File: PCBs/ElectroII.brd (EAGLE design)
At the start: 114.3 x 76.2 mm, 35 parts, among them J1 U.FL-R-SMT(01), T1 VIN, T2 VBAT, T3 GND, T4 5V, T5 VCC, U1 RFM95W-868S2, U2 TPS61090RSAR

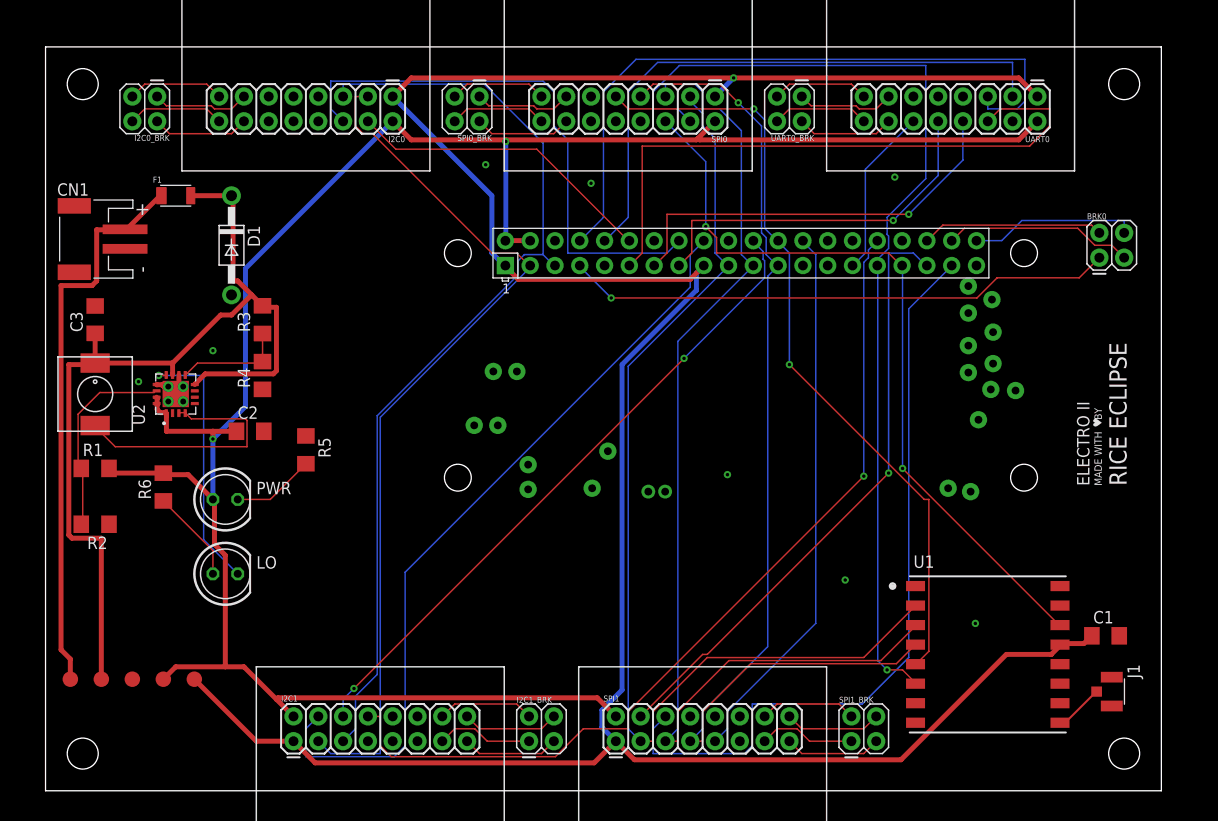
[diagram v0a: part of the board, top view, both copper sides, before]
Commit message: Fixed MOSI/MISO mistake
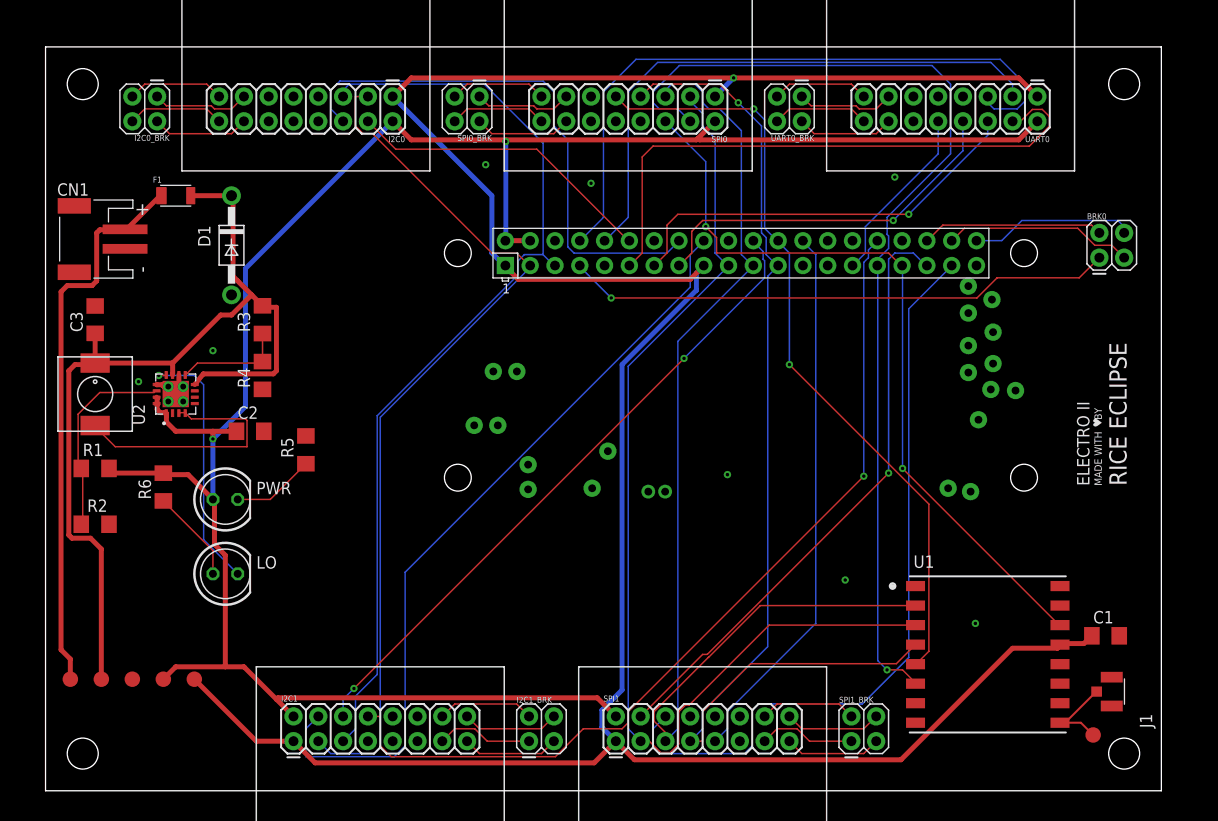
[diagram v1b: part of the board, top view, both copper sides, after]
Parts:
- added T6: ANT, RTR Main Library:TEST_PAD
- C2: value 100u -> 47u
- R1: value 1.85M -> 1.8M
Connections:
- net ANT: now also T6.P$1
- net MISO: now also U1.2; no longer U1.3
- net MOSI: now also U1.3; no longer U1.2
- net UART0_GPIO0: now also UART0.4; no longer UART0.6
- net UART0_GPIO1: now also UART0.6; no longer UART0.8
- net UART0_GPIO2: now also UART0.8; no longer UART0.10
- net UART0_GPIO3: now also UART0.10; no longer UART0.12
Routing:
- net ANT: track 5.07 -> 8.98 mm
- net UART0_GPIO0: track 64.0 -> 60.3 mm
- net SPI0_GPIO0: track 103.2 -> 105.3 mm
- net TX: track 70.5 -> 68.7 mm
- net MISO: track 111.2 -> 112.9 mm
- net RX: track 60.4 -> 59.1 mm
- net VBAT: track 95.4 -> 94.2 mm
- net UART0_GPIO3: track 17.4 -> 18.4 mm
- net I2C0_GPIO1: track 57.0 -> 56.1 mm
- net SPI1_GPIO1: track 79.1 -> 78.3 mm
- net 5V: track 222.9 -> 222.4 mm
- net VIN: track 57.9 -> 57.3 mm
- net N$2: track 27.2 -> 26.6 mm

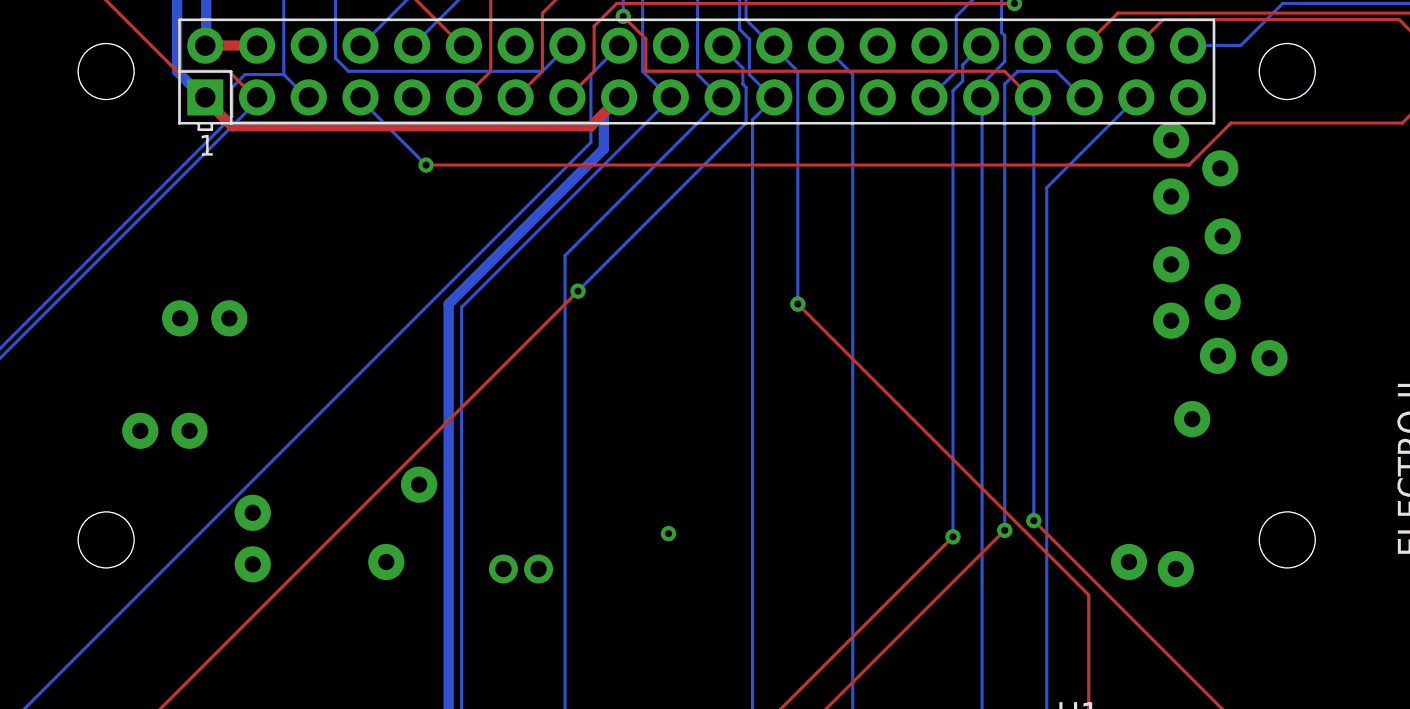
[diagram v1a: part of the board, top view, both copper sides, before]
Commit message: Updated RPi library
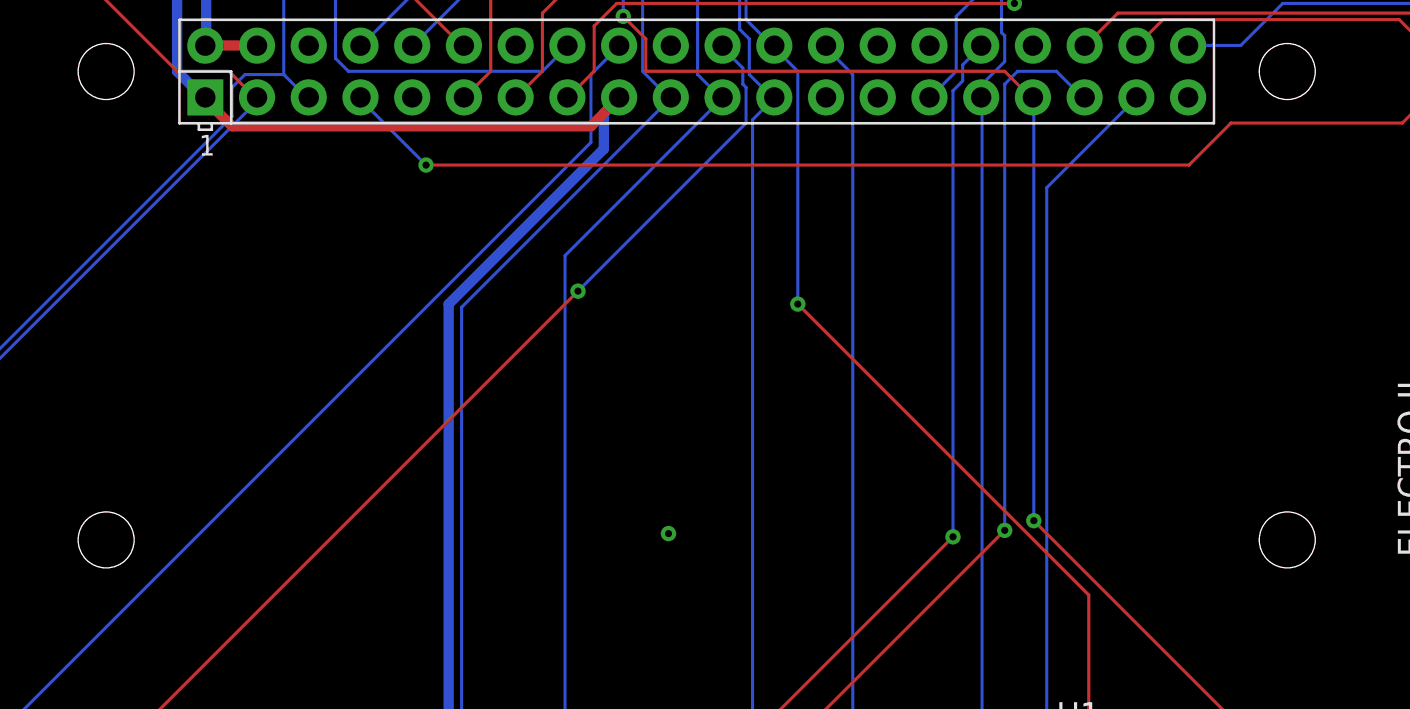
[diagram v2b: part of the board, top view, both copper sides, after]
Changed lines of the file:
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@@
 <wire x1="11.94450625" y1="41.5922" x2="12.13470625" y2="41.402" width="0.508" layer="1"/>
 <wire x1="12.13470625" y1="41.402" x2="12.573" y2="41.402" width="0.508" layer="1"/>
+<wire x1="86.995" y1="62.865" x2="88.9" y2="71.12" width="0" layer="19" extent="1-1"/>
+<wire x1="87.745" y1="56.345" x2="86.995" y2="62.865" width="0" layer="19" extent="1-1"/>
+<wire x1="82.665" y1="56.345" x2="87.745" y2="56.345" width="0" layer="19" extent="1-1"/>
+<wire x1="77.585" y1="53.805" x2="82.665" y2="56.345" width="0" layer="19" extent="1-1"/>
+<wire x1="95.365" y1="53.805" x2="87.745" y2="56.345" width="0" layer="19" extent="1-1"/>
+<wire x1="69.965" y1="56.345" x2="77.585" y2="53.805" width="0" layer="19" extent="1-1"/>
+<wire x1="62.345" y1="56.345" x2="69.965" y2="56.345" width="0" layer="19" extent="1-1"/>
+<wire x1="57.265" y1="53.805" x2="62.345" y2="56.345" width="0" layer="19" extent="1-1"/>
+<wire x1="52.185" y1="56.345" x2="57.265" y2="53.805" width="0" layer="19" extent="1-1"/>
+<wire x1="55.88" y1="62.23" x2="52.185" y2="56.345" width="0" layer="19" extent="1-1"/>
+<wire x1="55.88" y1="71.12" x2="55.88" y2="62.23" width="0" layer="19" extent="1-1"/>
+<wire x1="45.085" y1="64.135" x2="52.185" y2="56.345" width="0" layer="19" extent="1-1"/>
+<wire x1="69.85" y1="32.385" x2="77.585" y2="53.805" width="0" layer="19" extent="1-1"/>
+<wire x1="81.915" y1="21.59" x2="69.85" y2="32.385" width="0" layer="19" extent="1-1"/>
+<wire x1="89.12" y1="20.97" x2="81.915" y2="21.59" width="0" layer="19" extent="1-1"/>
+<wire x1="95.25" y1="17.145" x2="89.12" y2="20.97" width="0" layer="19" extent="1-1"/>
+<wire x1="89.12" y1="6.97" x2="95.25" y2="17.145" width="0" layer="19" extent="1-1"/>
+<wire x1="103.92" y1="8.97" x2="95.25" y2="17.145" width="0" layer="19" extent="1-1"/>
+<wire x1="109.22" y1="8.685" x2="103.92" y2="8.97" width="0" layer="19" extent="1-1"/>
+<wire x1="109.22" y1="11.635" x2="109.22" y2="8.685" width="0" layer="19" extent="1-1"/>
+<wire x1="109.985" y1="15.875" x2="109.22" y2="11.635" width="0" layer="19" extent="1-1"/>
+<wire x1="71.12" y1="5.08" x2="89.12" y2="6.97" width="0" layer="19" extent="1-1"/>
+<wire x1="22.86" y1="71.12" x2="45.085" y2="64.135" width="0" layer="19" extent="1-1"/>
+<wire x1="19.05" y1="50.8" x2="22.86" y2="71.12" width="0" layer="19" extent="1-1"/>
+<wire x1="17.145" y1="45.085" x2="19.05" y2="50.8" width="0" layer="19" extent="1-1"/>
+<wire x1="13.66" y1="42.595" x2="17.145" y2="45.085" width="0" layer="19" extent="1-1"/>
+<wire x1="13.335" y1="40.64" x2="14.097" y2="41.402" width="0" layer="19" extent="1-1"/>
+<wire x1="14.097" y1="39.878" x2="13.335" y2="40.64" width="0" layer="19" extent="1-1"/>
+<wire x1="12.573" y1="39.878" x2="13.335" y2="40.64" width="0" layer="19" extent="1-1"/>
+<wire x1="15.29" y1="39.665" x2="14.097" y2="39.878" width="0" layer="19" extent="1-1"/>
+<wire x1="15.29" y1="40.315" x2="15.29" y2="39.665" width="0" layer="19" extent="1-1"/>
+<wire x1="15.29" y1="40.965" x2="15.29" y2="40.315" width="0" layer="19" extent="1-1"/>
+<wire x1="9.525" y1="41.91" x2="11.38" y2="41.615" width="0" layer="19" extent="1-1"/>
+<wire x1="22.225" y1="41.123" x2="17.145" y2="45.085" width="0" layer="19" extent="1-1"/>
+<wire x1="22.355" y1="36.83" x2="22.225" y2="41.123" width="0" layer="19" extent="1-1"/>
+<wire x1="26.67" y1="36.347" x2="22.355" y2="36.83" width="0" layer="19" extent="1-1"/>
+<wire x1="5.08" y1="49.66" x2="9.525" y2="41.91" width="0" layer="19" extent="1-1"/>
+<wire x1="8.145" y1="55.515" x2="5.08" y2="49.66" width="0" layer="19" extent="1-1"/>
+<wire x1="6.502" y1="27.305" x2="12.573" y2="39.878" width="0" layer="19" extent="1-1"/>
+<wire x1="8.89" y1="11.43" x2="6.502" y2="27.305" width="0" layer="19" extent="1-1"/>
+<wire x1="38.1" y1="5.08" x2="8.89" y2="11.43" width="0" layer="19" extent="1-1"/>
 </signal>
 <signal name="MOSI">

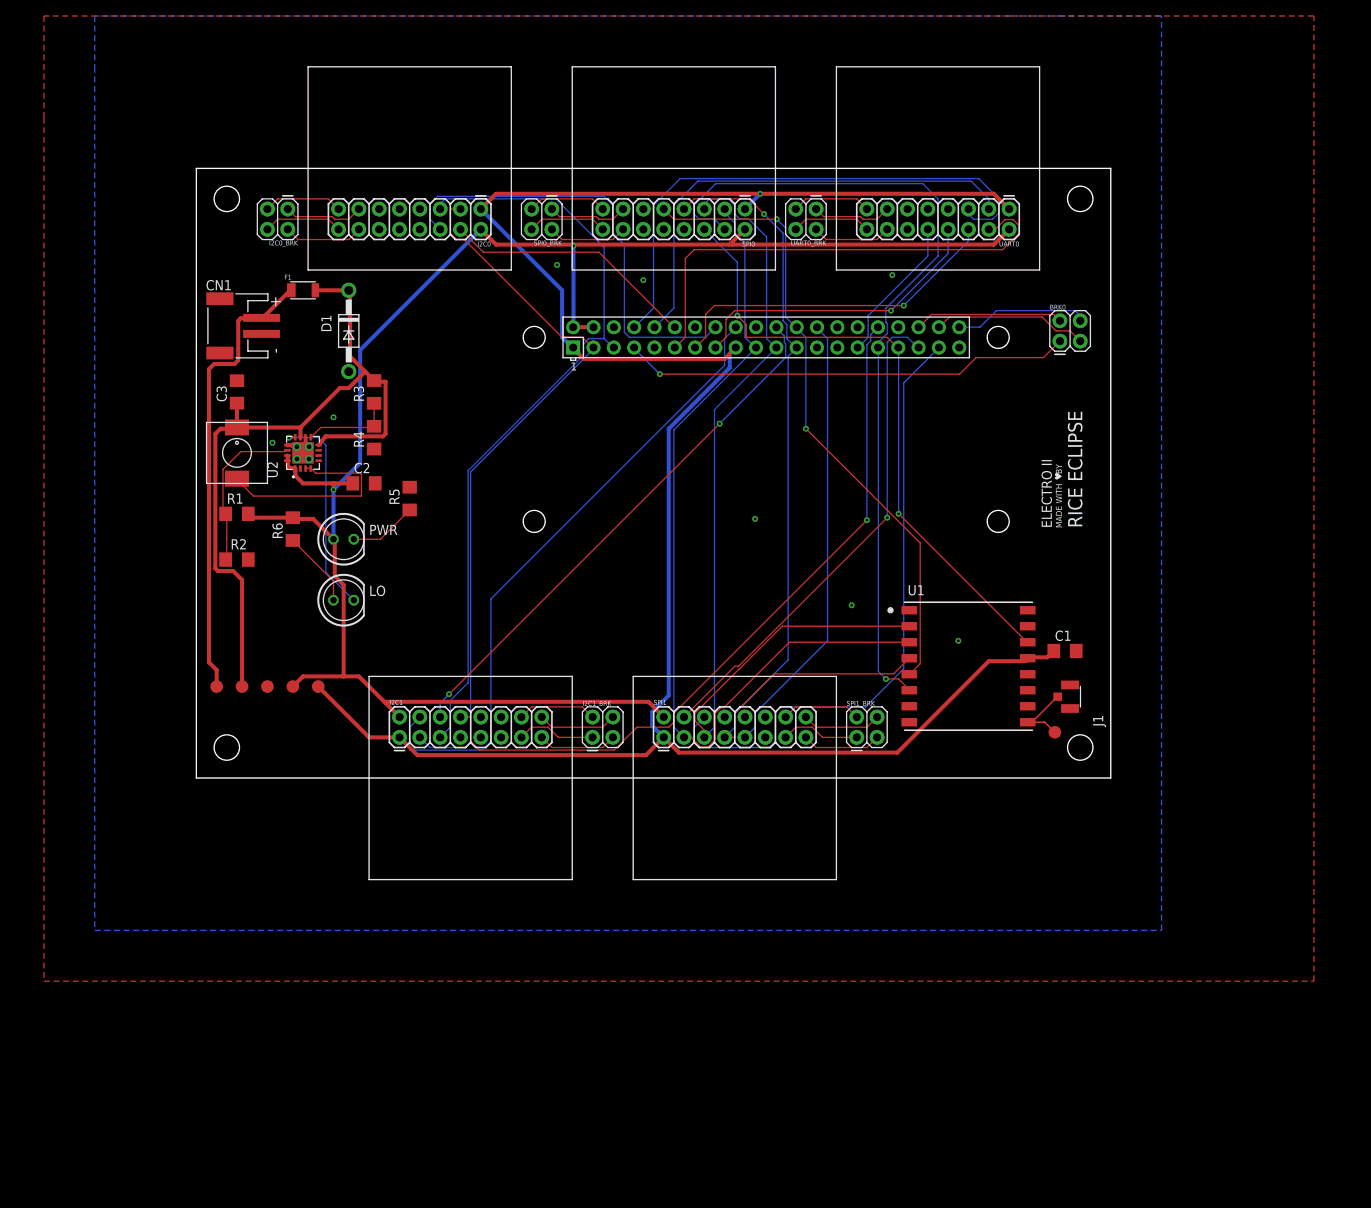
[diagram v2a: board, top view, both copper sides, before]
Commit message: Board shake-ups from design review
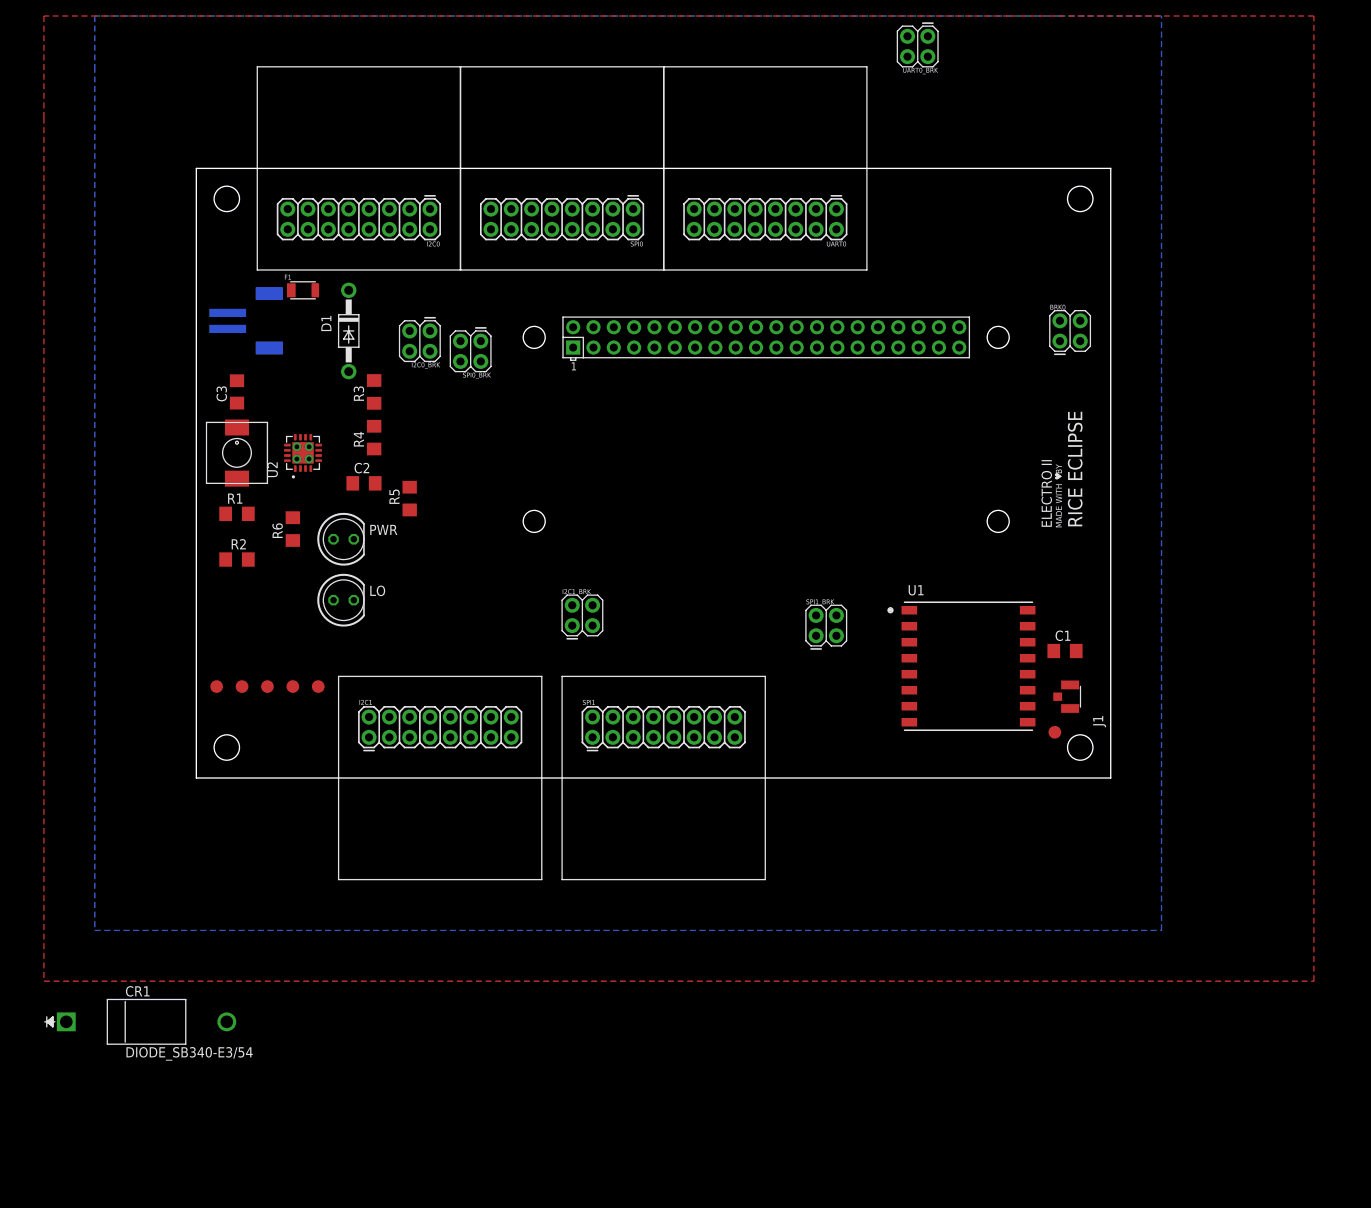
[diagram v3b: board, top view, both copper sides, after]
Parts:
- added CR1: DIODE_SB340-E3/54, DIODE_SB340-E3-54:DIODE_DO-201AD
- R1: value 1.8M -> 2M
- moved UART0_BRK 25.7 mm to (90.2, 91.4)
- moved I2C0_BRK 23.4 mm to (27.9, 54.6)
- moved UART0 21.6 mm to (71.1, 76.2)
- moved SPI0_BRK 18.8 mm to (34.3, 53.3)
- moved I2C1_BRK 14.2 mm to (48.3, 20.3)
- moved SPI0 14.0 mm to (45.7, 76.2)
- moved SPI1_BRK 13.7 mm to (78.7, 19.1)
- moved SPI1 8.89 mm to (58.4, 0.00)
- moved I2C0 6.35 mm to (20.3, 76.2)
- moved I2C1 3.81 mm to (30.5, 0.00)
- moved CN1 3.24 mm to (7.62, 57.1), flipped to the bottom
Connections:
- new net BOOST_OUT: C2.1, CR1.2, PWR.A, R1.2, R6.2, T4.P$1, U2.1, U2.15, U2.16
- net 5V: now also CR1.1; no longer C2.1, PWR.A, R1.2, R6.2, T4.P$1, U2.1, U2.15, U2.16
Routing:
- net VCC: track 270.2 -> 0.00 mm, vias 1 -> 0
- net 5V: track 222.4 -> 0.00 mm, vias 2 -> 0
- net MISO: track 112.9 -> 0.00 mm
- net SCLK: track 111.1 -> 0.00 mm, vias 1 -> 0
- net MOSI: track 108.5 -> 0.00 mm
- net SPI0_GPIO0: track 105.3 -> 0.00 mm, vias 1 -> 0
- net SCL: track 96.4 -> 0.00 mm
- net VBAT: track 94.2 -> 0.00 mm
- net I2C1_GPIO2: track 91.5 -> 0.00 mm, vias 1 -> 0
- net SDA: track 91.0 -> 0.00 mm
- net I2C1_GPIO0: track 79.7 -> 0.00 mm
- net CE0: track 79.6 -> 0.00 mm, vias 2 -> 0
- net SPI0_GPIO1: track 78.8 -> 0.00 mm, vias 2 -> 0
- net SPI1_GPIO1: track 78.3 -> 0.00 mm
- net TX: track 68.7 -> 0.00 mm
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
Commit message: More board shuffling
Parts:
- added R7, R8: DNP, RTR Main Library:R1206
- added R9: 0.1 1/8w, RTR Main Library:R1206
- T4: value 5V -> BOOST
- T6: value ANT -> 5V
- moved T6 125.4 mm to (-10.2, -38.1)
- moved I2C1 87.0 mm to (72.4, 76.2), turned to 180 degrees
- moved UART0 84.1 mm to (35.6, 0.00), turned to 0 degrees
- moved J1 62.7 mm to (101.6, 72.4), turned to 90 degrees
- moved C1 53.6 mm to (95.9, 67.9), turned to 180 degrees
- moved U1 43.3 mm to (99.1, 57.1), turned to 90 degrees
- moved I2C1_BRK 43.3 mm to (20.3, -12.7)
- moved BRK0 37.5 mm to (142.2, 38.1)
- moved SPI0_BRK 33.1 mm to (36.8, 20.3), turned to 270 degrees
- moved U$1 14.8 mm to (46.4, 15.9)
- moved SPI1 2.54 mm to (61.0, 0.00)
- moved SPI0 1.27 mm to (47.0, 76.2)
- moved I2C0 1.27 mm to (21.6, 76.2)
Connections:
- removed net I2C0_GPIO1: I2C0.6, U$1.16
- new net CGND: R9.1
- new net SPI2_GPIO0: U$1.18, U1.6
- new net SPI2_GPIO1: U$1.16, U1.14
- net 5V: now also T6.P$1
- net ANT: no longer T6.P$1
- net GND: now also R9.2
- net I2C0_GPIO0: no longer I2C0.4
- net I2C1_GPIO0: no longer U$1.18
- net SCL: now also R8.1
- net SDA: now also R7.1
- net SPI0_GPIO0: no longer U1.6
- net SPI0_GPIO1: no longer U1.14
- net VCC: now also R7.2, R8.2
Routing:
- net ANT: track 0.00 -> 9.63 mm
